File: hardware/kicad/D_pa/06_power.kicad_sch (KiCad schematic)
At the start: 47 parts, among them J30 50V giris, J31 A kartina, J32 C kartindan, Q30 IRF9540N, Q31 2N7002, Q32 2N7002, U50 LM5164DDAR, U51 TPS62130, U55 MCP9700AT, U56 74HC595D, U57 MCP3208T-CI/SL

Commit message: Update the hardware tools and add the gateware
This commit makes the public tree equal to the development tree. The
public tree was behind. It did not have the verification tools, the
build chain, or the FPGA source.

The hardware/kicad directory now has the full tool chain. This
includes yap.sh, which runs the steps in the correct order, and the
tools that check the boards.

The gateware directory is new. It has the Verilog source for the
Lattice ECP5, the test benches, and the synthesis script. The
gateware does the four-channel receive chain, the transmit chain, the
packet interface, and the control interface.

The internal Turkish documents stay in the development tree. The
documentation in this repository is English. The comments in the
source code stay in Turkish.
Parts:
- added J33: sonraki PA, Connector_PinHeader_2.54mm:PinHeader_2x10_P2.54mm_Vertical, symbol Connector_Generic:Conn_02x10_Odd_Even
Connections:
- net +3V3: now also J33.1 (Pin_1)
- net ADC_SDIO: now also J33.7 (Pin_7)
- net ATT_CLK: now also J33.5 (Pin_5)
- net ATT_DATA: now also J33.3 (Pin_3)
- net GND: now also J33.10 (Pin_10), J33.12 (Pin_12), J33.14 (Pin_14), J33.16 (Pin_16), J33.17 (Pin_17), J33.18 (Pin_18), J33.19 (Pin_19), J33.2 (Pin_2), J33.20 (Pin_20), J33.4 (Pin_4), J33.6 (Pin_6), J33.8 (Pin_8)
- net PA_INHIBIT: now also J33.15 (Pin_15)
- net RLY_RCLK: now also J33.13 (Pin_13)
- net RLY_SRCLK: now also J33.11 (Pin_11)
- net RLY_SER_NEXT: now reaches U56.9 (QH')
- net RLY_SER_NEXT: now also J33.9 (Pin_9)
- no-connect marks 5 -> 4
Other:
- note added: "DORT PA'YA KADAR BUYUR, A KARTINDA EK PIN ISTEMEDEN. Paylasilan: ATT_DATA, ATT_CLK, ADC_SDIO. Bunlar veri yolu, her kart ayni hatti dinliyor. Karta ozel olan secme sinyalleri (ATT_LE, BIAS_CS, ADC_CS) FPGA'dan gelmiyor — her kart kendi 74HC595'inden uretiyor. Zincir A -> C -> D1 -> D2 -> D3 -> D4 diye uzuyor ve ek kart basina FPGA'da TEK PIN bile harcanmiyor. PA_INHIBIT ZINCIRE GIRMIYOR, dogrudan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"
- note added: "SONRAKI PA KARTINA — ZINCIR GECISI"

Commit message: Connect the pads that had no net
A symbol pin number must agree with the footprint pad number. If the
numbers do not agree, the net goes nowhere. The netlist removes it
and gives no message. ERC examines the schematic and sees a wire. DRC
does not count an unconnected pad as a violation. All three boards
showed zero ERC violations while 31 pads had no net.

Two of these faults stopped a board.

The footprint of the Ethernet PHY was for a different part. The
project used QFN-48 6x6 mm with 0.4 mm pitch. The RTL8211F(I)-CG is
WQFN-40-EP 5x5 mm. You cannot solder the part to that pad pattern.

The 25 MHz crystal had a 2-pin symbol on a 4-pad footprint. On a 3225
crystal the terminals are the diagonal pads 1 and 3. Pads 2 and 4 are
the metal can. XO went to pad 2. There was no crystal between XI and
XO, and thus neither PHY could make a clock.

The paddle of the AD9251 was pin 0 in the symbol and pad 65 in the
footprint. The paddle of the PE4312 was Pad against pad 21. The gas
discharge tubes had one electrode unconnected, because
Device:GDT_2Pin uses pins 1 and 3 but the varistor footprint uses
pads 1 and 2. A local footprint with pads 1 and 3 corrects this.

ped_denetim.py finds these faults on the board. yap.sh runs it before
the DSN export. The chain stops if a pad has no net.

The DSN export also changed. It declared In1 and In4 as power layers
but did not export the copper on them. The router thus believed that
the two ground planes were empty. It routed the 289 pins of GND as
traces on the signal layers. The planes now go out as conduction
areas.
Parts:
- removed C603, C606, C612, C616, C624: 100nF, Capacitor_SMD:C_0603_1608Metric, symbol Device:C
- removed C605, C611: 22uF, Capacitor_SMD:C_0603_1608Metric, symbol Device:C
- removed D30: 15V, Diode_SMD:D_SOD-323, symbol Device:D_Zener
- removed D617, D618, D619, D620, D621, D622, D623: 1N4148WS, Diode_SMD:D_SOD-323, symbol Device:D
- removed Q30: IRF9540N, Package_TO_SOT_THT:TO-220-3_Vertical, symbol Transistor_FET:Q_PMOS_GSD
- removed R600, R613, R615: 100k, Resistor_SMD:R_0603_1608Metric, symbol Device:R
- removed R607: 140k, Resistor_SMD:R_0603_1608Metric, symbol Device:R
- removed R609: 105k, Resistor_SMD:R_0603_1608Metric, symbol Device:R
- removed R610: 20k, Resistor_SMD:R_0603_1608Metric, symbol Device:R
- added C600, C609, C617, C651, C660, C665, C667: 100nF, Capacitor_SMD:C_0603_1608Metric, symbol Device:C
- added C650: 10uF, Capacitor_SMD:C_1206_3216Metric, symbol Device:C
- added C661: 22nF, Capacitor_SMD:C_0805_2012Metric, symbol Device:C
- added C662: 100nF, Capacitor_SMD:C_0805_2012Metric, symbol Device:C
- added C663: 2.2uF, Capacitor_SMD:C_1210_3225Metric, symbol Device:C
- added C664: 22uF, Capacitor_SMD:C_1206_3216Metric, symbol Device:C
- added C666: 22uF, Capacitor_SMD:C_0603_1608Metric, symbol Device:C
- added D31: SMBJ54A, Diode_SMD:D_SMB, symbol Device:D_TVS
- added D607, D610, D611, D612, D613, D615, D616: 1N4148WS, Diode_SMD:D_SOD-323, symbol Device:D
- added Q30: IRFB4110PBF, Package_TO_SOT_THT:TO-220-3_Vertical, symbol Transistor_FET:Q_NMOS_GDS
- added R601, R606: 100k, Resistor_SMD:R_0603_1608Metric, symbol Device:R
- added R602: 140k, Resistor_SMD:R_0603_1608Metric, symbol Device:R
- added R603: 10k, Resistor_SMD:R_0603_1608Metric, symbol Device:R
- added R605: 20k, Resistor_SMD:R_0603_1608Metric, symbol Device:R
- added U52: LM74700QDBVRQ1, Package_TO_SOT_SMD:SOT-23-6, symbol Power_Management:LM74700
- C601, C602: footprint Capacitor_THT:CP_Radial_D10.0mm_P5.00mm -> Capacitor_THT:CP_Radial_D16.0mm_P7.50mm
- R604: value 100k -> 105k
- R608: value 10k -> 100k
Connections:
- net +12V: now also D614.2 (A), C650.1, C651.1, C664.1, C665.1, D610.2 (A), D611.2 (A), D612.2 (A), D613.2 (A), D615.2 (A), D616.2 (A), R602.1
- net +3V3: now also C609.1, C617.1
- net +50V: now also C662.1, C663.1, Q30.2 (D), U52.4 (CATHODE)
- net +5V: now also R604.1, C666.1, C667.1, D607.2 (A); no longer D614.2 (A)
- net BST_12V: now also C600.1
- net DPD_EN: now also R606.1
- net DPD_EN_LO: now also D607.1 (K); no longer D614.1 (K)
- net FB_12V: now also R602.2, R603.1; no longer R608.1
- net FB_5V: now also R604.2, R605.1
- net GND: now also C609.2, C617.2, C650.2, C651.2, C661.2, C662.2, C663.2, C664.2, C665.2, C666.2, C667.2, D31.2 (A2), R601.2, R603.2, R605.2, R606.2, U52.2 (GND); no longer R604.2
- net KL1_LO: now also D610.1 (K)
- net KL2_LO: now also D611.1 (K)
- net KL3_LO: now also D612.1 (K)
- net KL4_LO: now also D613.1 (K)
- net KL5_LO: now also D614.1 (K)
- net KL6_LO: now also D615.1 (K)
- net KL7_LO: now also D616.1 (K)
- net PA_INHIBIT: now also R608.1
- net RON_12V: now also R601.1; no longer R604.1
- net SW_12V: now also C600.2
- net VIN50: now also C660.2, C661.1, D31.1 (A1), Q30.3 (S), U52.3 (EN), U52.6 (ANODE)
- net VIN50_G: now also Q30.1 (G), U52.5 (GATE)
- new net VCAP50: C660.1, U52.1 (VCAP)
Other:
- note added: "TERS POLARITE — IDEAL DIYOT (LM74700-Q1 + IRFB4110) Eski cozum IRF9540N P-MOSFET'ti: 0.117 ohm x 6.67 A^2 = 5.2 W. Sogutucusuz TO-220'de 320 C artis demek, yani parca 100 W'lik ilk veriste olurdu. Simdi 3.7 mohm x 6.67 A^2 = 0.17 W; sogutucu gerekmiyor, kartin ortasinda durabilir. 15 V zener KALKTI: gecit gerilimini artik denetleyici sinirliyor (VCAP-ANODE en fazla 13 V, IRFB4110 Vgs sinirlari +-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"
- note removed: "Ters polarite: P-MOSFET, A kartindakinin ayni mantigi ama buyugu. 6.7 A gectigi icin TO-220 ve dusuk Rds(on). Zener Vgs'i 15 V'ta sinirliyor (50 V rayda -50 V gorurdu)."

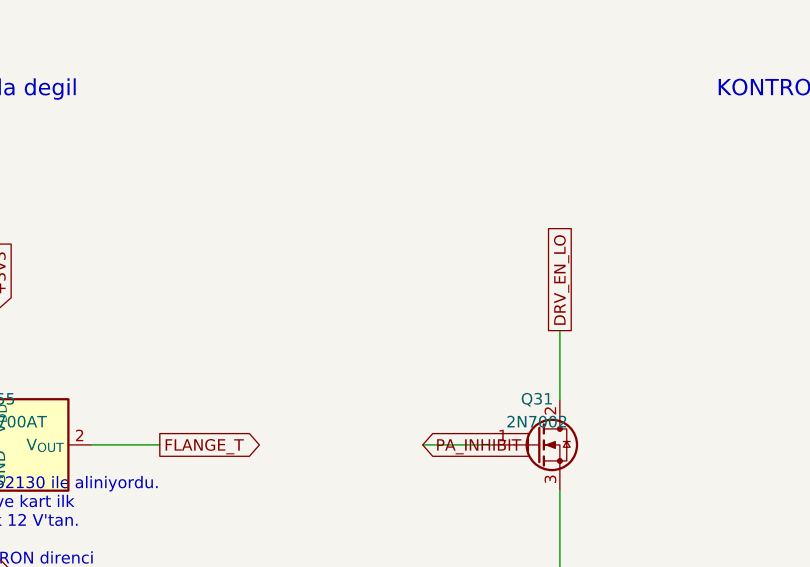
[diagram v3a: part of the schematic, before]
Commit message: Correct the clearance test for the pre-routed traces
The clearance test used a circle for each pad. The radius was
max(width, height)/2. The corner of a rectangle is at
hypot(width, height)/2 from the center. The test thus made the pad
smaller than it is. On the 2.5 x 4.5 mm gate pad of a TO-247 the
difference is 2.250 mm against 2.574 mm.

The DRN_A trace was on the gate pad of Q10 with an overlap of 35 um.
This is a short circuit between the 50 V drain rail and the gate of a
100 W device. The search that finds the tee offset accepted this
route. The overlap is at a corner and 35 um wide. You cannot see it
on a plot.

The test now uses the real shape of the pad and the collision test of
pcbnew. It also uses the 300 um clearance and not only an overlap. A
trace that is 50 um from a pad is also not possible to manufacture.

Board D was built again. No trace is below 300 um and the smallest
gap is 0.537 mm. Boards A and C were correct.
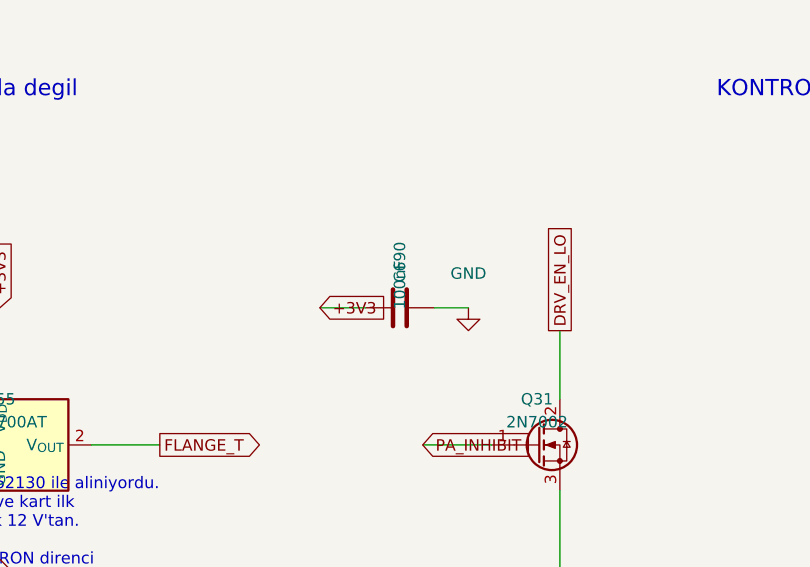
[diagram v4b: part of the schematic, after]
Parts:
- added C690: 100nF, Capacitor_SMD:C_0603_1608Metric, symbol Device:C
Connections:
- net +3V3: now also C690.1
- net GND: now also C690.2
